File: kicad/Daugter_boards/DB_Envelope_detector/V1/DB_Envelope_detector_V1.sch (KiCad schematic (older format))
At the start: 5 parts

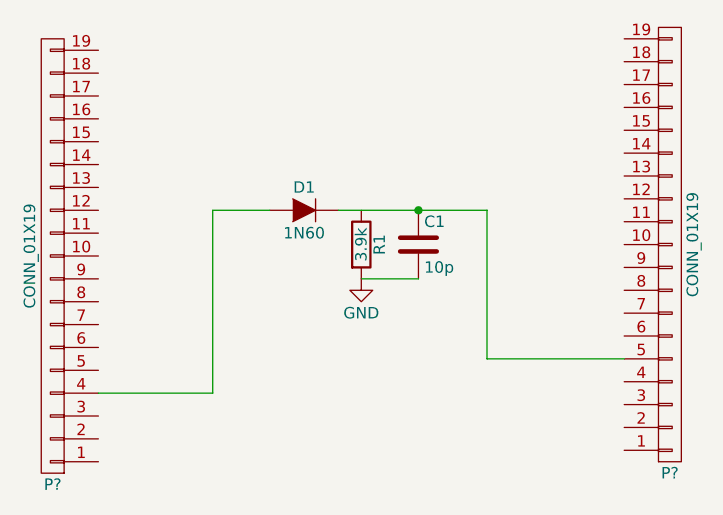
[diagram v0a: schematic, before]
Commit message: DB envelope detector, motor control, pulser
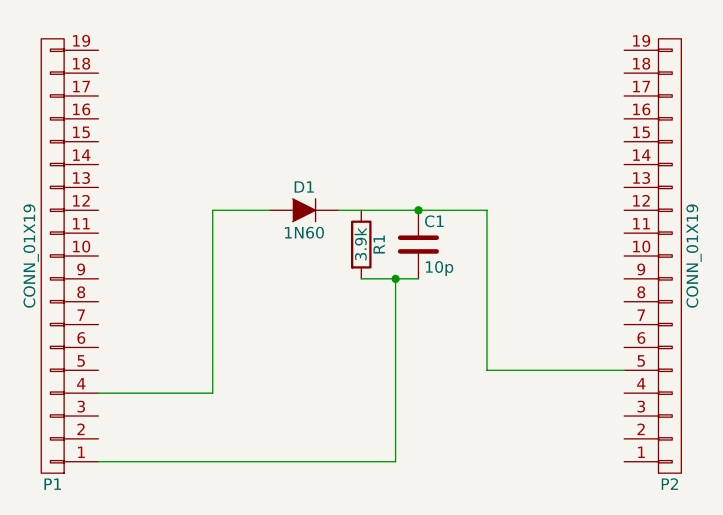
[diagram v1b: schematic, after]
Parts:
- gave numbers to parts that had none: 2
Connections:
- net GND is gone; now on an unnamed net: C1.2, R1.2
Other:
- moved on the sheet: P2
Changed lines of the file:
@@
 LIBS:contrib
 LIBS:valves
+LIBS:DB_Envelope_detector_V1-cache
 EELAYER 25 0
 EELAYER END
@@
 	3350 2500 3600 2500
 $Comp
-L GND #PWR1
-U 1 1 57A4D5CE
-P 3350 2500
-F 0 "#PWR1" H 3350 2250 50  0001 C CNN
-F 1 "GND" H 3350 2350 50  0000 C CNN
-F 2 "" H 3350 2500 50  0000 C CNN
-F 3 "" H 3350 2500 50  0000 C CNN
-	1    3350 2500
-	1    0    0    -1
-$EndComp
-$Comp
-L CONN_01X19 P?
+L CONN_01X19 P1
 U 1 1 57A857B8
 P 2000 2400
-F 0 "P?" H 2000 3400 50  0000 C CNN
+F 0 "P1" H 2000 3400 50  0000 C CNN
 F 1 "CONN_01X19" V 2100 2400 50  0000 C CNN
 F 2 "" H 2000 2400 50  0000 C CNN
@@
 $EndComp
 $Comp
-L CONN_01X19 P?
+L CONN_01X19 P2
 U 1 1 57A857FF
-P 4700 2350
-F 0 "P?" H 4700 3350 50  0000 C CNN
-F 1 "CONN_01X19" V 4800 2350 50  0000 C CNN
-F 2 "" H 4700 2350 50  0000 C CNN
-F 3 "" H 4700 2350 50  0000 C CNN
-	1    4700 2350
+P 4700 2400
+F 0 "P2" H 4700 3400 50  0000 C CNN
+F 1 "CONN_01X19" V 4800 2400 50  0000 C CNN
+F 2 "" H 4700 2400 50  0000 C CNN
+F 3 "" H 4700 2400 50  0000 C CNN
+	1    4700 2400
 	1    0    0    1
 $EndComp
@@
 	2700 2200 2950 2200
 Wire Wire Line
-	4500 2850 3900 2850
+	3900 2900 4500 2900
 Wire Wire Line
-	3900 2850 3900 2200
+	3900 2200 3900 2900
 Connection ~ 3600 2200
+Wire Wire Line
+	3500 2500 3500 3300
+Wire Wire Line
+	3500 3300 2200 3300
+Connection ~ 3500 2500
 $EndSCHEMATC

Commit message: update daugter boards
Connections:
- net at C1.2, P1.1 (P1), R1.2: now also P2.1 (P1)
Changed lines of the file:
@@
 	3500 2500 3500 3300
 Wire Wire Line
-	3500 3300 2200 3300
+	2200 3300 4500 3300
 Connection ~ 3500 2500
+Connection ~ 3500 3300
 $EndSCHEMATC
